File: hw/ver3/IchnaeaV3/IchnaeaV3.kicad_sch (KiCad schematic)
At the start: 25 parts, among them J1 Screw_Terminal_01x09, J2 Screw_Terminal_01x09, J3 Screw_Terminal_01x09, J8 Screw_Terminal_01x09, U15 INA180A4

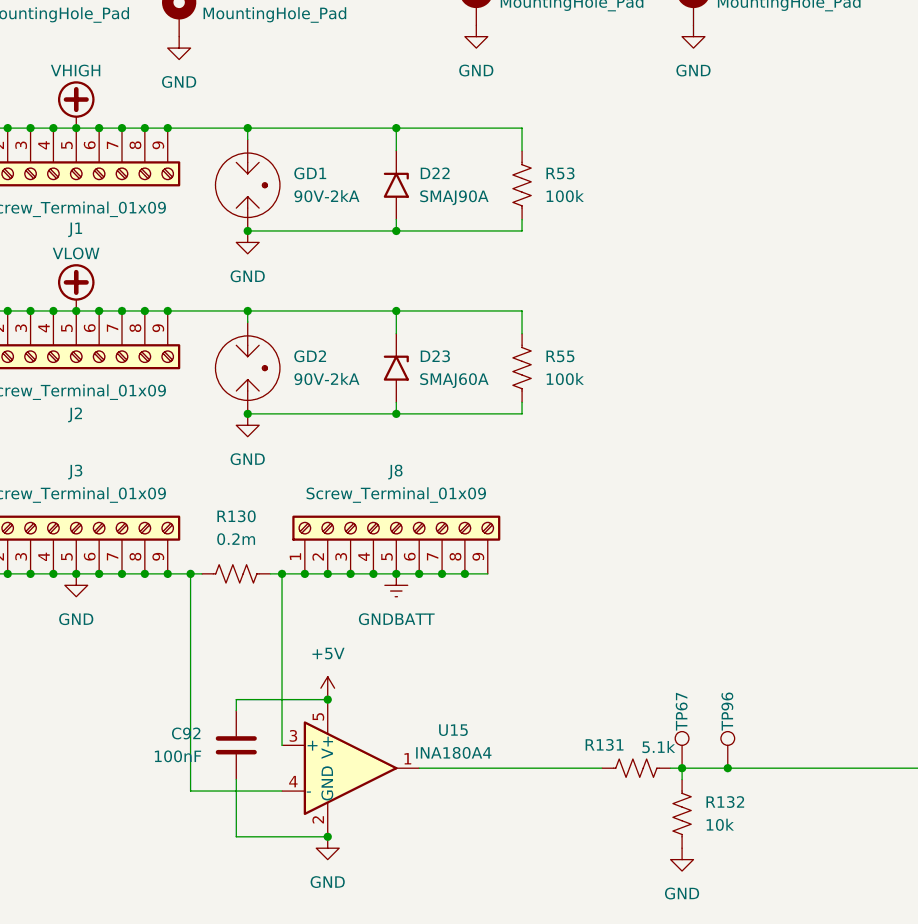
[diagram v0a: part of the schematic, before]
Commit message: Experiment with a new power stage layout
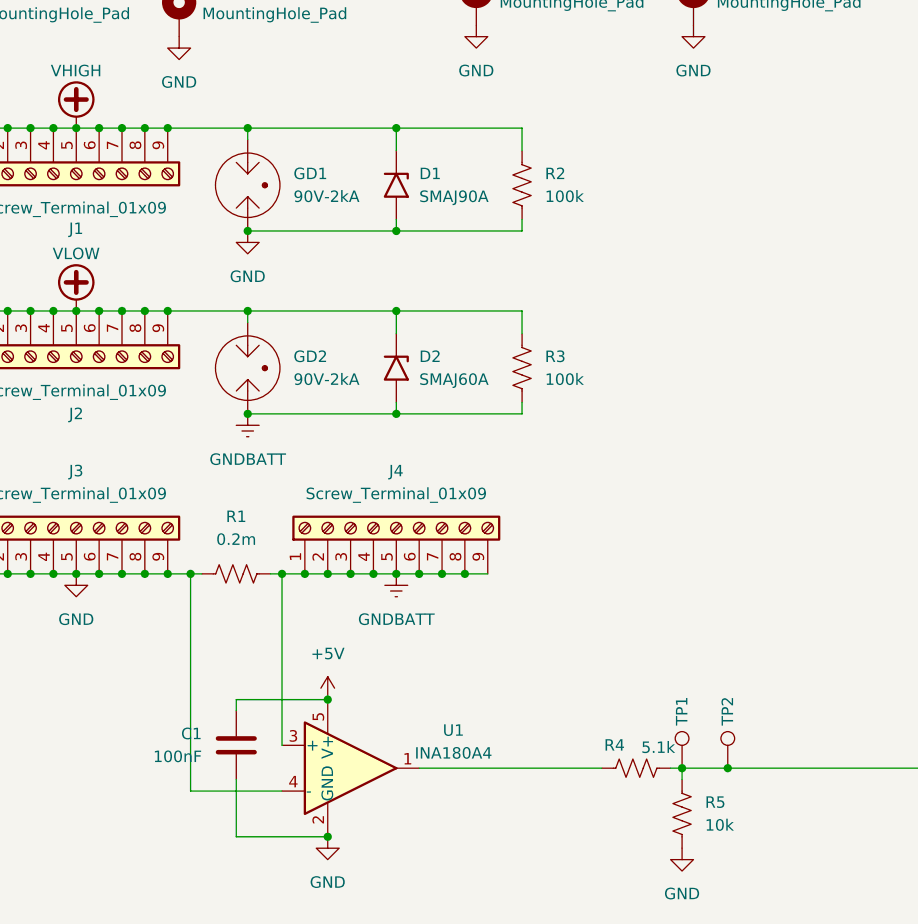
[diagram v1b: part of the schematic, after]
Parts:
- renumbered C92 to C1, D22 to D1, D23 to D2, J8 to J4, R130 to R1, R53 to R2, R55 to R3, R131 to R4, R132 to R5, TP67 to TP1, TP96 to TP2, U15 to U1
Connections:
- net GND: no longer D2.2 (A2), GD2.1, R3.2
- net GNDBATT: now also D2.2 (A2), GD2.1, R3.2
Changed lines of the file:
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@@
 	)
 	(junction
-		(at 25.4 52.07)
+		(at 52.07 83.82)
 		(diameter 0)
 		(color 0 0 0 0)
 	)
 	(junction
-		(at 25.4 72.39)
+		(at 25.4 52.07)
 		(diameter 0)
 		(color 0 0 0 0)
 	)
 	(junction
-		(at 33.02 101.6)
+		(at 25.4 72.39)
 		(diameter 0)
 		(color 0 0 0 0)
 	)
 	(junction
-		(at 52.07 83.82)
+		(at 33.02 101.6)
 		(diameter 0)
 		(color 0 0 0 0)
@@
 		(dnp no)
 		(fields_autoplaced yes)
-		(property "Reference" "#PWR0223"
+		(property "Reference" "#PWR011"
 			(at 60.96 137.16 0)
 			(effects
@@
 			(project "IchnaeaV3"
 				(path "/93408532-1ffa-463d-873c-16289d2b7987"
-					(reference "#PWR0223")
+					(reference "#PWR011")
 					(unit 1)
 				)
@@
 	)
 	(symbol
+		(lib_id "power:GNDREF")
+		(at 52.07 83.82 0)
+		(unit 1)
+		(exclude_from_sim no)
+		(in_bom yes)
+		(on_board yes)
+		(dnp no)
+		(fields_autoplaced yes)
+		(property "Reference" "#PWR09"
+			(at 52.07 90.17 0)
+			(effects
+				(font
+					(size 1.27 1.27)
+				)
+				(hide yes)
+			)
+		)
+		(property "Value" "GNDBATT"
+			(at 52.07 88.9 0)
+			(effects
+				(font
+					(size 1.27 1.27)
+				)
+			)
+		)
+		(property "Footprint" ""
+			(at 52.07 83.82 0)
+			(effects
+				(font
+					(size 1.27 1.27)
+				)
+				(hide yes)
+			)
+		)
+		(property "Datasheet" ""
+			(at 52.07 83.82 0)
+			(effects
+				(font
+					(size 1.27 1.27)
+				)
+				(hide yes)
+			)
+		)
+		(property "Description" "Power symbol creates a global label with name \"GNDREF\" , reference supply ground"
+			(at 52.07 83.82 0)
+			(effects
+				(font
+					(size 1.27 1.27)
+				)
+				(hide yes)
+			)
+		)
+		(pin "1"
+		)
+		(instances
+			(project "IchnaeaV3"
+				(path "/93408532-1ffa-463d-873c-16289d2b7987"
+					(reference "#PWR09")
+					(unit 1)
+				)
+			)
+		)
+	)
+	(symbol
 		(lib_id "Amplifier_Current:INA180A4")
 		(at 63.5 123.19 0)
@@
 		(dnp no)
 		(fields_autoplaced yes)
-		(property "Reference" "U15"
+		(property "Reference" "U1"
 			(at 74.93 118.999 0)
 			(effects
@@
 			(project "IchnaeaV3"
 				(path "/93408532-1ffa-463d-873c-16289d2b7987"
-					(reference "U15")
+					(reference "U1")
 					(unit 1)
 				)
@@
 		(on_board yes)
 		(dnp no)
-		(property "Reference" "C92"
+		(property "Reference" "C1"
 			(at 46.99 119.3799 0)
 			(effects
@@
 			(project "IchnaeaV3"
 				(path "/93408532-1ffa-463d-873c-16289d2b7987"
-					(reference "C92")
+					(reference "C1")
 					(unit 1)
 				)
@@
 		(on_board yes)
 		(dnp no)
-		(property "Reference" "R131"
+		(property "Reference" "R4"
 			(at 93.9799 120.65 90)
 			(effects
@@
 			(project "IchnaeaV3"
 				(path "/93408532-1ffa-463d-873c-16289d2b7987"
-					(reference "R131")
+					(reference "R4")
 					(unit 1)
 				)
@@
 		(dnp no)
 		(fields_autoplaced yes)
-		(property "Reference" "#PWR075"
+		(property "Reference" "#PWR016"
 			(at 101.6 34.29 0)
 			(effects
@@
 			(project "IchnaeaV3"
 				(path "/93408532-1ffa-463d-873c-16289d2b7987"
-					(reference "#PWR075")
+					(reference "#PWR016")
 					(unit 1)
 				)
@@
 		(dnp no)
 		(fields_autoplaced yes)
-		(property "Reference" "R53"
+		(property "Reference" "R2"
 			(at 85.09 57.1499 0)
 			(effects
@@
 			(project "IchnaeaV3"
 				(path "/93408532-1ffa-463d-873c-16289d2b7987"
-					(reference "R53")
+					(reference "R2")
 					(unit 1)
 				)
@@
 		(dnp no)
 		(fields_autoplaced yes)
-		(property "Reference" "#PWR0222"
+		(property "Reference" "#PWR012"
 			(at 68.58 107.95 0)
 			(effects
@@
 			(project "IchnaeaV3"
 				(path "/93408532-1ffa-463d-873c-16289d2b7987"
-					(reference "#PWR0222")
+					(reference "#PWR012")
 					(unit 1)
 				)
@@
 		(dnp no)
 		(fields_autoplaced yes)
-		(property "Reference" "#PWR059"
+		(property "Reference" "#PWR014"
 			(at 77.47 46.99 0)
 			(effects
@@
 			(project "IchnaeaV3"
 				(path "/93408532-1ffa-463d-873c-16289d2b7987"
-					(reference "#PWR059")
+					(reference "#PWR014")
 					(unit 1)
 				)
@@
 		(dnp no)
 		(fields_autoplaced yes)
-		(property "Reference" "D23"
+		(property "Reference" "D2"
 			(at 71.12 77.4699 90)
 			(effects
@@
 			(project "IchnaeaV3"
 				(path "/93408532-1ffa-463d-873c-16289d2b7987"
-					(reference "D23")
+					(reference "D2")
 					(unit 1)
 				)
@@
 		(dnp no)
 		(fields_autoplaced yes)
-		(property "Reference" "#PWR0220"
+		(property "Reference" "#PWR08"
 			(at 52.07 69.85 0)
 			(effects
@@
 			(project "IchnaeaV3"
 				(path "/93408532-1ffa-463d-873c-16289d2b7987"
-					(reference "#PWR0220")
+					(reference "#PWR08")
 					(unit 1)
 				)
@@
 		(dnp no)
 		(fields_autoplaced yes)
-		(property "Reference" "#PWR078"
+		(property "Reference" "#PWR017"
 			(at 101.6 46.99 0)
 			(effects
@@
 			(project "IchnaeaV3"
 				(path "/93408532-1ffa-463d-873c-16289d2b7987"
-					(reference "#PWR078")
+					(reference "#PWR017")
 					(unit 1)
 				)
@@
 		(on_board yes)
 		(dnp no)
-		(property "Reference" "#PWR092"
+		(property "Reference" "#PWR018"
 			(at 214.63 66.04 0)
 			(effects
@@
 			(project "IchnaeaV3"
 				(path "/93408532-1ffa-463d-873c-16289d2b7987"
-					(reference "#PWR092")
+					(reference "#PWR018")
 					(unit 1)
 				)
@@
 		(on_board yes)
 		(dnp no)
-		(property "Reference" "TP67"
+		(property "Reference" "TP1"
 			(at 100.33 116.84 90)
 			(effects
@@
 			(project "IchnaeaV3"
 				(path "/93408532-1ffa-463d-873c-16289d2b7987"
-					(reference "TP67")
+					(reference "TP1")
 					(unit 1)
 				)
@@
 		(dnp no)
 		(fields_autoplaced yes)
-		(property "Reference" "R132"
+		(property "Reference" "R5"
 			(at 102.87 126.9999 0)
 			(effects
@@
 			(project "IchnaeaV3"
 				(path "/93408532-1ffa-463d-873c-16289d2b7987"
-					(reference "R132")
+					(reference "R5")
 					(unit 1)
 				)
@@
 		(dnp no)
 		(fields_autoplaced yes)
-		(property "Reference" "#PWR055"
+		(property "Reference" "#PWR013"
 			(at 77.47 34.29 0)
 			(effects
@@
 			(project "IchnaeaV3"
 				(path "/93408532-1ffa-463d-873c-16289d2b7987"
-					(reference "#PWR055")
+					(reference "#PWR013")
 					(unit 1)
 				)
@@
 		(dnp no)
 		(fields_autoplaced yes)
-		(property "Reference" "R130"
+		(property "Reference" "R1"
 			(at 50.8 95.25 90)
 			(effects
@@
 			(project "IchnaeaV3"
 				(path "/93408532-1ffa-463d-873c-16289d2b7987"
-					(reference "R130")
+					(reference "R1")
 					(unit 1)
 				)
@@
 		(dnp no)
 		(fields_autoplaced yes)
-		(property "Reference" "R55"
+		(property "Reference" "R3"
 			(at 85.09 77.4699 0)
 			(effects
@@
 			(project "IchnaeaV3"
 				(path "/93408532-1ffa-463d-873c-16289d2b7987"
-					(reference "R55")
+					(reference "R3")
 					(unit 1)
 				)
@@
 		(dnp no)
 		(fields_autoplaced yes)
-		(property "Reference" "D22"
+		(property "Reference" "D1"
 			(at 71.12 57.1499 90)
 			(effects
@@
 			(project "IchnaeaV3"
 				(path "/93408532-1ffa-463d-873c-16289d2b7987"
-					(reference "D22")
+					(reference "D1")
 					(unit 1)
 				)
@@
 		(on_board yes)
 		(dnp no)
-		(property "Reference" "TP96"
+		(property "Reference" "TP2"
 			(at 105.41 116.84 90)
 			(effects
@@
 			(project "IchnaeaV3"
 				(path "/93408532-1ffa-463d-873c-16289d2b7987"
-					(reference "TP96")
+					(reference "TP2")
 					(unit 1)
 				)
@@
 		(dnp no)
 		(fields_autoplaced yes)
-		(property "Reference" "#PWR0225"
+		(property "Reference" "#PWR015"
 			(at 100.33 138.43 0)
 			(effects
@@
 			(project "IchnaeaV3"
 				(path "/93408532-1ffa-463d-873c-16289d2b7987"
-					(reference "#PWR0225")
+					(reference "#PWR015")
 					(unit 1)
 				)
@@
 		(dnp no)
 		(fields_autoplaced yes)
-		(property "Reference" "J8"
+		(property "Reference" "J4"
 			(at 68.58 90.17 90)
 			(effects
@@
 			(project "IchnaeaV3"
 				(path "/93408532-1ffa-463d-873c-16289d2b7987"
-					(reference "J8")
+					(reference "J4")
 					(unit 1)
 				)
@@
 		(dnp no)
 		(fields_autoplaced yes)
-		(property "Reference" "#PWR0224"
+		(property "Reference" "#PWR010"
 			(at 60.96 119.38 0)
 			(effects
@@
 			(project "IchnaeaV3"
 				(path "/93408532-1ffa-463d-873c-16289d2b7987"
-					(reference "#PWR0224")
-					(unit 1)
-				)
-			)
-		)
-	)
-	(symbol
-		(lib_id "power:GND")
-		(at 52.07 83.82 0)
-		(unit 1)
-		(exclude_from_sim no)
-		(in_bom yes)
-		(on_board yes)
-		(dnp no)
-		(fields_autoplaced yes)
-		(property "Reference" "#PWR0221"
-			(at 52.07 90.17 0)
-			(effects
-				(font
-					(size 1.27 1.27)
-				)
-				(hide yes)
-			)
-		)
-		(property "Value" "GND"
-			(at 52.07 88.9 0)
-			(effects
-				(font
-					(size 1.27 1.27)
-				)
-			)
-		)
-		(property "Footprint" ""
-			(at 52.07 83.82 0)
-			(effects
-				(font
-					(size 1.27 1.27)
-				)
-				(hide yes)
-			)
-		)
-		(property "Datasheet" ""
-			(at 52.07 83.82 0)
-			(effects
-				(font
-					(size 1.27 1.27)
-				)
-				(hide yes)
-			)
-		)
-		(property "Description" "Power symbol creates a global label with name \"GND\" , ground"
-			(at 52.07 83.82 0)
-			(effects
-				(font
-					(size 1.27 1.27)
-				)
-				(hide yes)
-			)
-		)
-		(pin "1"
-		)
-		(instances
-			(project "IchnaeaV3"
-				(path "/93408532-1ffa-463d-873c-16289d2b7987"
-					(reference "#PWR0221")
+					(reference "#PWR010")
 					(unit 1)
 				)

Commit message: Swiftly correct the design issue.
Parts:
- removed J1, J2, J3, J4: Screw_Terminal_01x09, Connectors:CONN_74651195R_WRE, symbol Connector:Screw_Terminal_01x09
- removed TP1, TP2: TestPoint, TestPoint:TestPoint_Pad_D1.0mm, symbol Connector:TestPoint
- added C101, C102, C103, C104, C105: 100nF, Capacitor_SMD:C_0603_1608Metric, symbol Device:C
- added J1, J2: Terminal Block, symbol Connector:Screw_Terminal_01x02
- added R95: 0.2m, Resistors:Shunt_5930, symbol Device:R_US
- added R96: 5.1k, Resistor_SMD:R_0603_1608Metric, symbol Device:R_US
- added R97: 10k, Resistor_SMD:R_0603_1608Metric, symbol Device:R_US
- added U19: INA180A4, Package_TO_SOT_SMD:SOT-23-5, symbol Amplifier_Current:INA180A4
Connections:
- net GNDBATT is gone; now on net GND: D2.2 (A2), GD2.1, R1.2, R3.2, U1.3 (+)
- net +5V: now also C101.1, U19.5 (V+)
- net GND: now also C101.2, C102.2, C103.1, C104.1, C105.1, R95.2, R97.1, U19.2 (GND), U19.3 (+); no longer R1.1, U1.4 (-)
- net ControlStage/CTL_IN_ADC_IBATT_SENSE renamed ISENSE_OUTPUT
- net ISENSE_OUTPUT: now also C103.2
- net VHIGH renamed VIN
- net VIN: now also J1.1 (Pin_1)
- net VLOW renamed VOUT
- net VOUT: now also J2.1 (Pin_1)
- new net: C105.2, J1.2 (Pin_2), R95.1, U19.4 (-)
- new net: C104.2, J2.2 (Pin_2), R1.1, U1.4 (-)
- new net: R96.2, U19.1
- new net ISENSE_INPUT: C102.1, R96.1, R97.2
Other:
- sheet ControlStage ports: added ISENSE_PWR_IN, ISENSE_PWR_OUT; removed CTL_IN_ADC_IBATT_SENSE, CTL_IN_SDI, CTL_LTC_IMON, CTL_LTC_PWM_EN, CTL_OUT_CSB, CTL_OUT_SCK, CTL_OUT_SDO
- sheet PowerStage ports: added IO_LOAD_SW_EN; removed IO_LTC_IMON
- moved on the sheet: C1, D1, D2, GD1, GD2, H1, H2, H3, H4, H5, H6, H7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

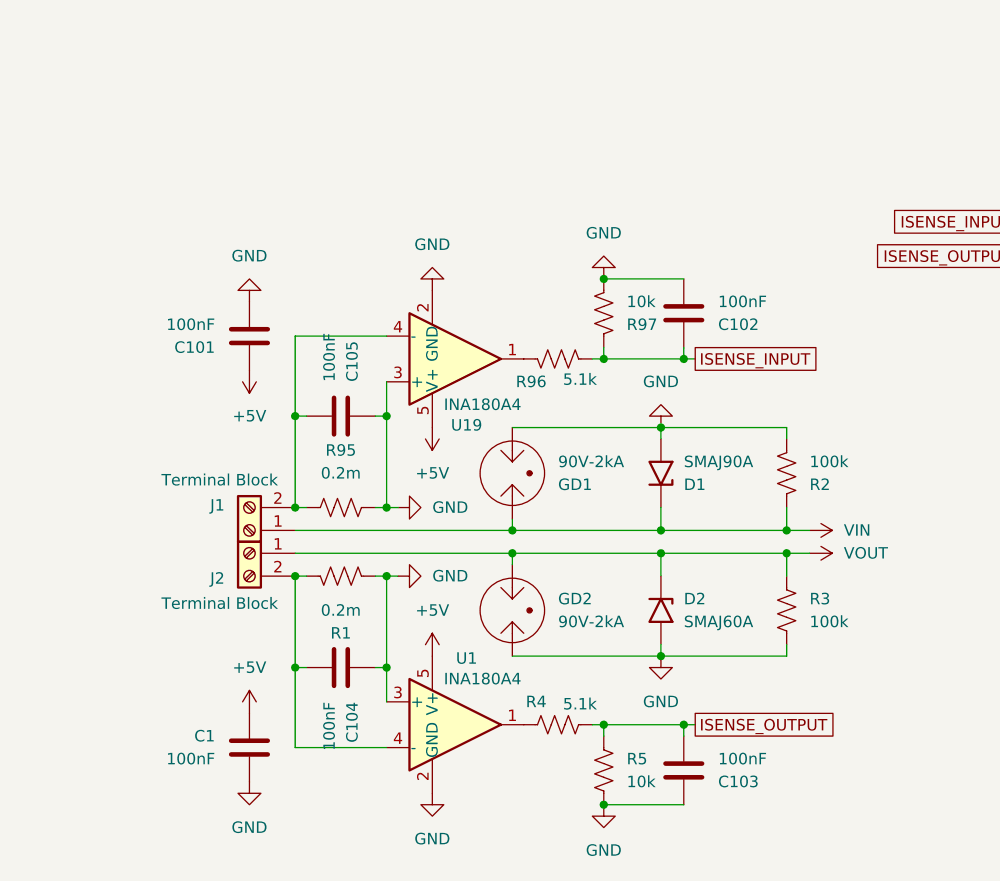
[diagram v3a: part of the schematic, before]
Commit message: Cost optimize power terminal connections
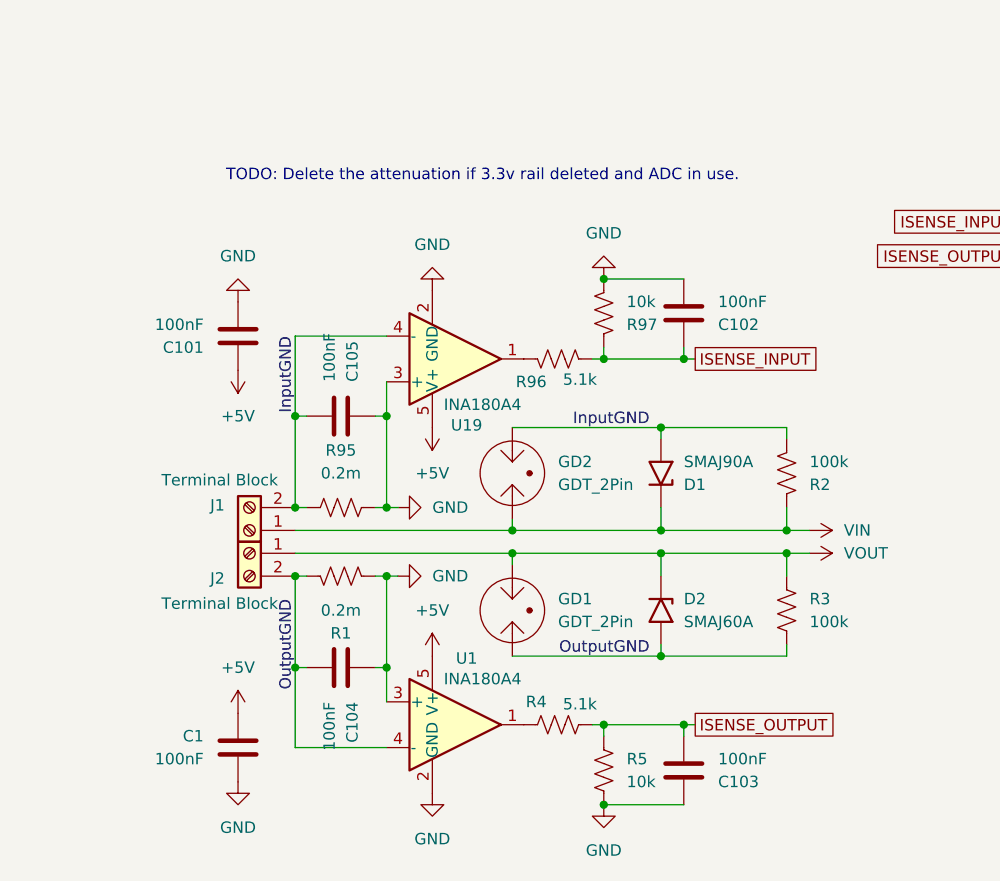
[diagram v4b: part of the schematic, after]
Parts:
- GD1, GD2: value 90V-2kA -> GDT_2Pin
- J1, J2: footprint (none) -> Connectors:KF88SA-16.0-2P
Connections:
- net GND: no longer D1.2 (A2), D2.2 (A2), GD1.1, GD2.1, R2.2, R3.2
- net VIN: now also GD2.1; no longer GD1.2
- net VOUT: now also GD1.2; no longer GD2.2
- net InputGND: now reaches C105.2, J1.2 (Pin_2), R95.1, U19.4 (-)
- net InputGND: now also D1.2 (A2), GD2.2, R2.2
- net OutputGND: now reaches C104.2, J2.2 (Pin_2), R1.1, U1.4 (-)
- net OutputGND: now also D2.2 (A2), GD1.1, R3.2
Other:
- note added: "TODO: Delete the attenuation if 3.3v rail deleted and ADC in use."
- moved on the sheet: C1, C101
